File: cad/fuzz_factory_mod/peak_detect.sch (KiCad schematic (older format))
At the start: 46 parts

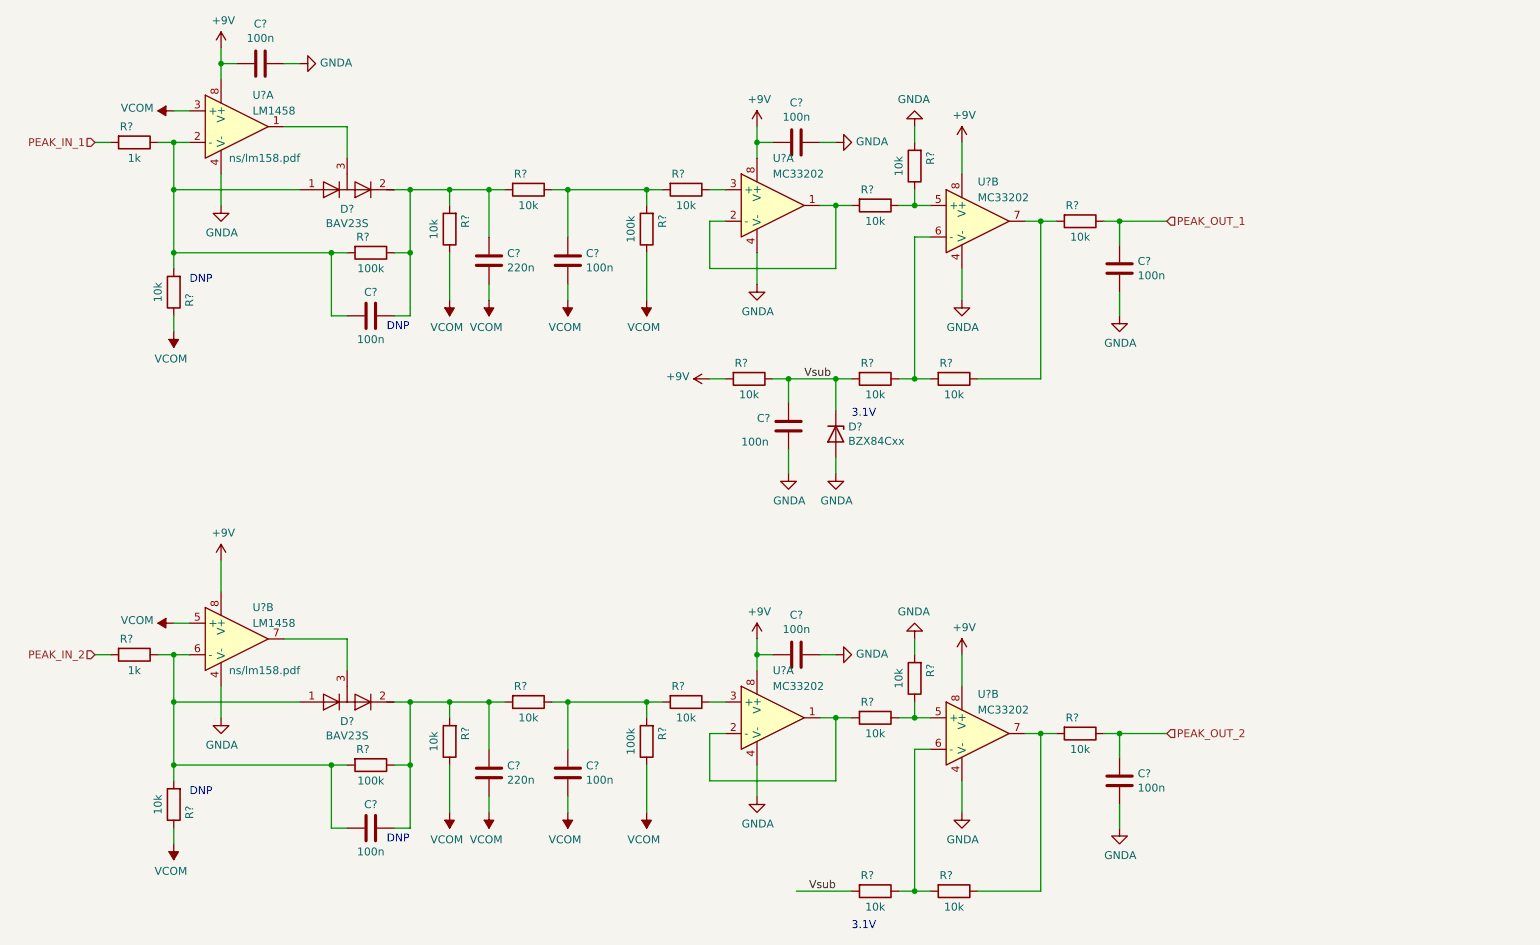
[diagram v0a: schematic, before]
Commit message: Modified OPA repartition on peak detector.
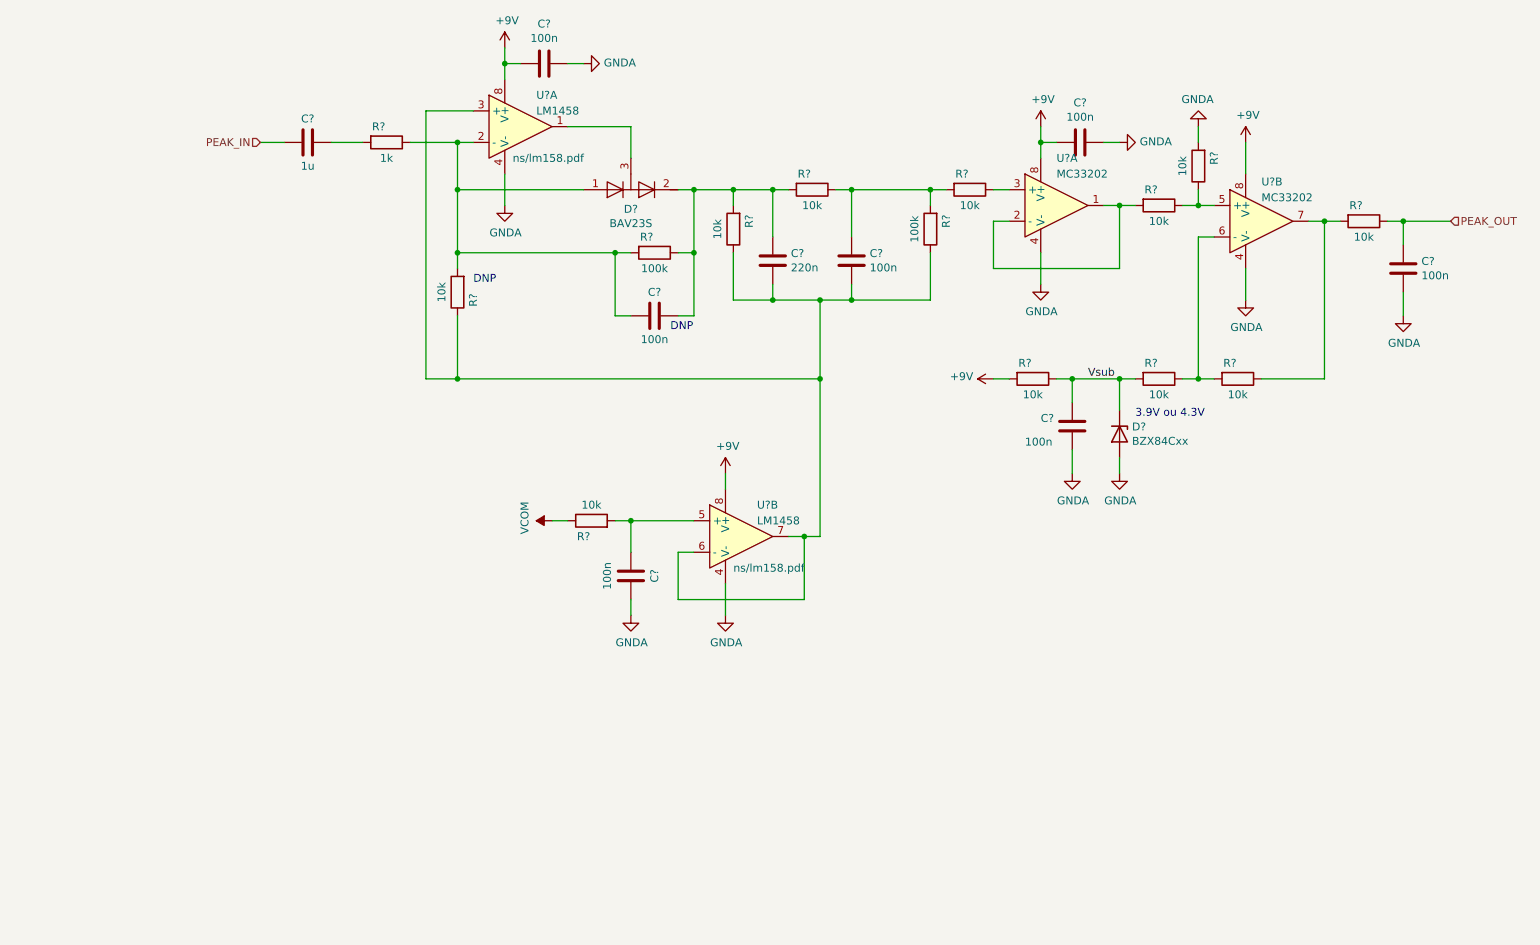
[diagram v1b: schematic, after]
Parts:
- removed C? (x4): 100n, symbol Device:C
- removed C?: 220n, symbol Device:C
- removed D?: BAV23S, symbol flax_lib:BAV23S
- removed R? (x2): 100k, symbol Device:R
- removed R?: 1k, symbol Device:R
- removed R? (x9): 10k, symbol Device:R
- removed U? (x2): MC33202, symbol flax_lib:MC33202
- added C?: 100n, symbol Device:C
- added C?: 1u, symbol Device:C
- added R?: 10k, symbol Device:R
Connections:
- net GNDA: now also C?.1
- net VCOM: now also R?.1; no longer C?.2, C?.2, R?.1, R?.1, R?.1, U?.3 (+), U?.5 (+)
- net at U?.6 (-): now also C?.2, C?.2, R?.1, R?.1, R?.1, U?.3 (+), U?.7
- net PEAK_IN_1: no longer names the net of R?.2
- net PEAK_IN_1: now also C?.1
- net PEAK_OUT_1 renamed PEAK_OUT
- new net: C?.2, R?.2, U?.5 (+)
- new net PEAK_IN: C?.2
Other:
- note added: "3.9V ou 4.3V"
- note removed: "3.1V"
- moved on the sheet: C?, D?, R?, U?A, U?B

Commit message: Continued schematic.
Modified fuuz_factory circuit : use of matched transistor pairs.
Added USB interface, through FT230X and direct to MCU.
Associated footprints, except for XTAL and trimmers.
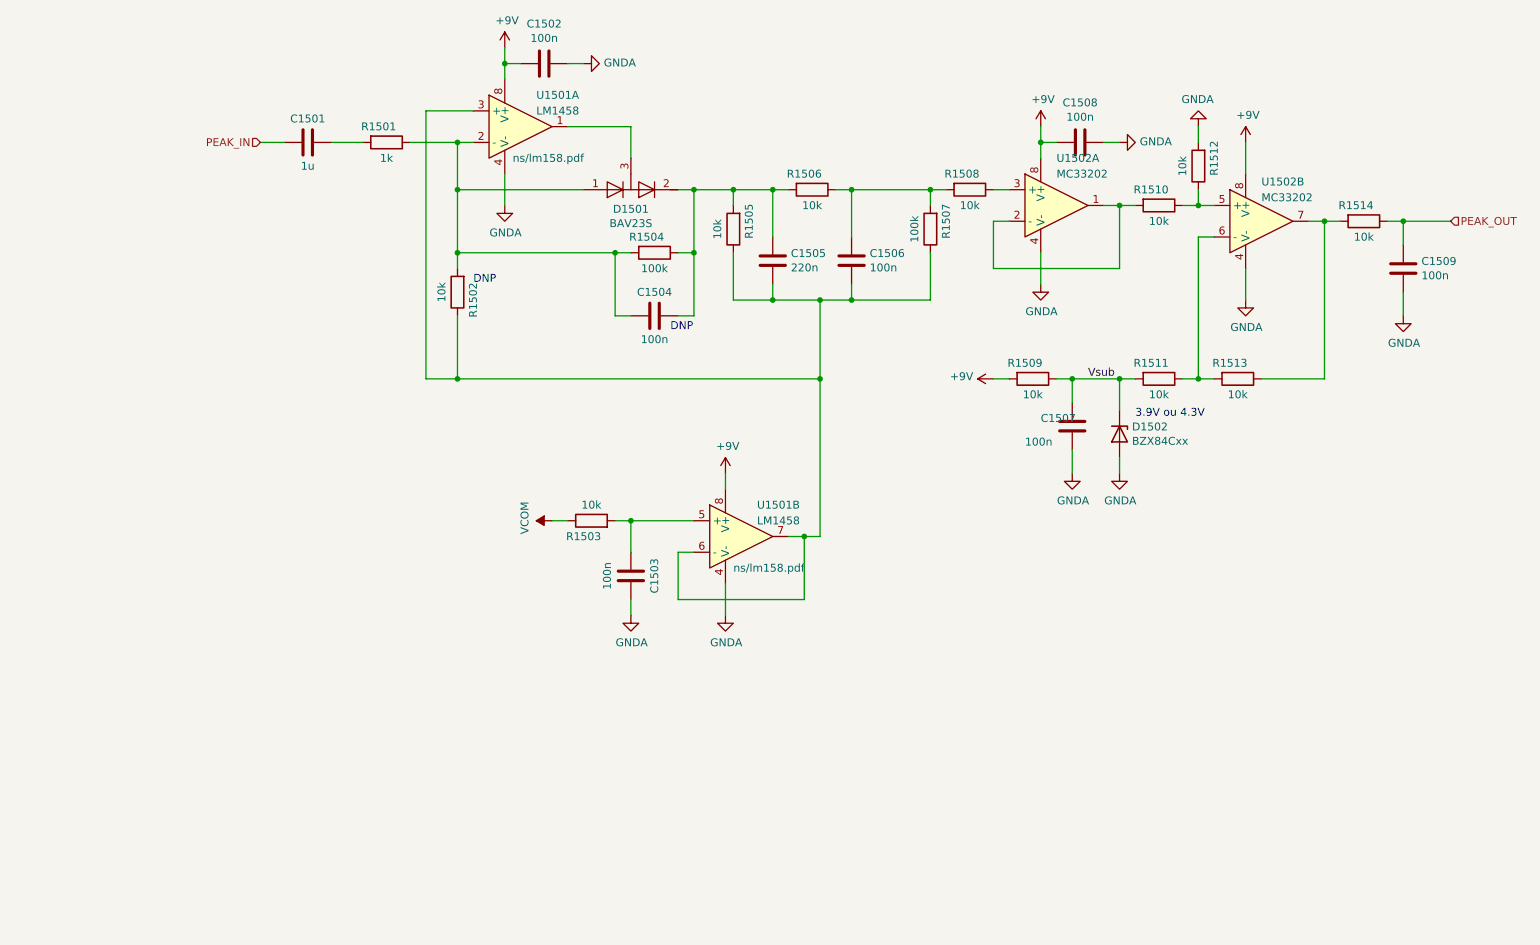
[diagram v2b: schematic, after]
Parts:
- C1101, C1105: renamed from C?; footprint (none) -> Capacitors_SMD:C_0805
- C1102, C1103, C1104, C1106, C1107, C1108, C1109: renamed from C?; footprint (none) -> Capacitors_SMD:C_0603
- D1101: renamed from D?; footprint (none) -> TO_SOT_Packages_SMD:SOT-23
- R1101, R1102, R1103, R1104, R1105, R1106, R1107, R1108, R1110, R1111, R1112, R1113, R1114: renamed from R?; footprint (none) -> Resistors_SMD:R_0603
- R1109: renamed from R?; footprint (none) -> Resistors_SMD:R_0805
- U1101, U1102: renamed from U?; footprint (none) -> Housings_SOIC:SOIC-8_3.9x4.9mm_Pitch1.27mm
- gave numbers to parts that had none: 1

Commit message: Continued schematic.
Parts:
- D1102: footprint Diode_SMD:D_SOT-23_ANK -> Diodes_SMD:D_SOT-23_ANK

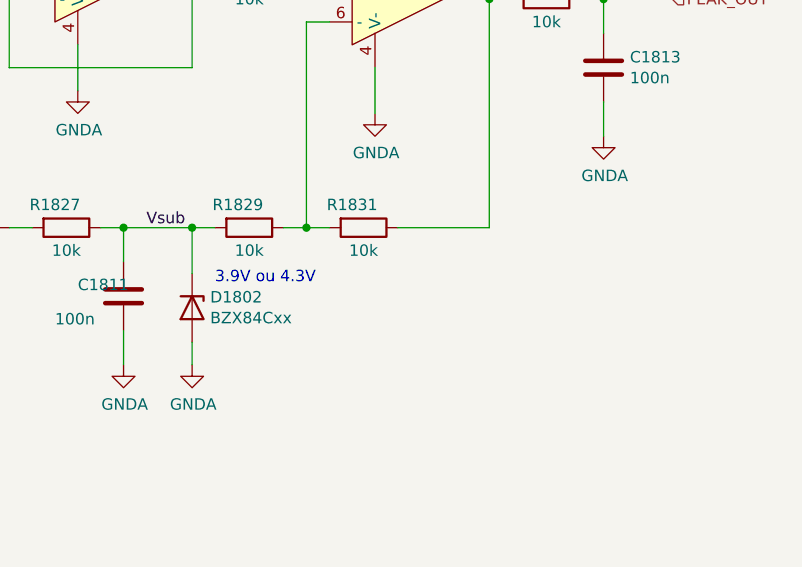
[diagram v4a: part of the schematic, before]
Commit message: Continued schematic.
Continued component placement.
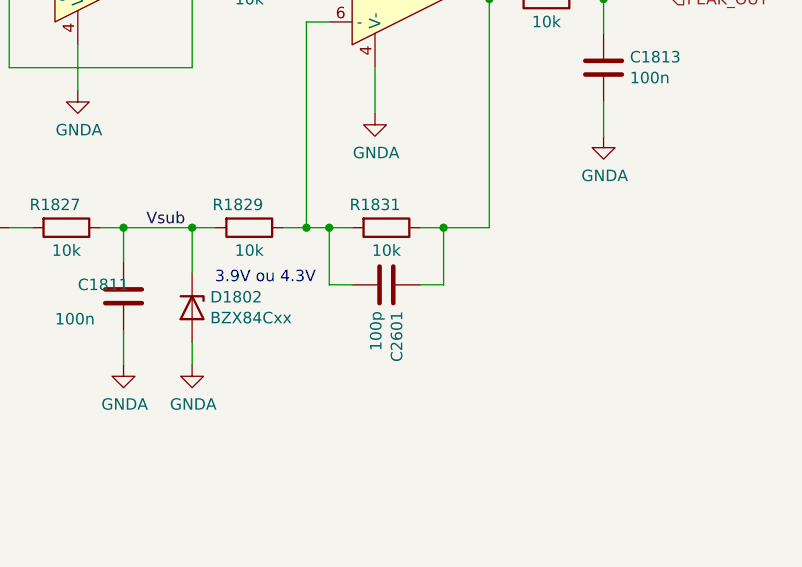
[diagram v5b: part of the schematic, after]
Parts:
- added C1901: 100p, Capacitors_SMD:C_0603, symbol Device:C
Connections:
- net at R1111.1, R1113.2, U1102.6 (-): now also C1901.2
- net at R1113.1, R1114.2, U1102.7: now also C1901.1
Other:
- moved on the sheet: R1831
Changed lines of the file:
@@
 $Descr A4 11693 8268
 encoding utf-8
-Sheet 11 30
+Sheet 19 30
 Title ""
 Date ""
@@
 L Device:R R1113
 U 1 1 5E6C867B
-P 8950 3000
+P 9050 3000
 AR Path="/5DE4AD88/5E68EE8E/5E6C867B" Ref="R1113"  Part="1"
 AR Path="/5DE4AD88/5EB8346E/5E6C867B" Ref="R1513"  Part="1"
 AR Path="/5DE4AD88/5EE3A0D9/5E6C867B" Ref="R1715"  Part="1"
 AR Path="/5DE4AD88/5EE3A870/5E6C867B" Ref="R1831"  Part="1"
-F 0 "R1831" V 8850 2950 50  0000 C CNN
-F 1 "10k" V 9050 3000 50  0000 C CNN
-F 2 "Resistors_SMD:R_0603" V 8880 3000 50  0001 C CNN
-F 3 "~" H 8950 3000 50  0001 C CNN
-	1    8950 3000
+F 0 "R1831" V 8950 2950 50  0000 C CNN
+F 1 "10k" V 9150 3000 50  0000 C CNN
+F 2 "Resistors_SMD:R_0603" V 8980 3000 50  0001 C CNN
+F 3 "~" H 9050 3000 50  0001 C CNN
+	1    9050 3000
 	0    1    1    0
 $EndComp
@@
 Connection ~ 8200 1900
 Wire Wire Line
-	8800 3000 8700 3000
-Wire Wire Line
-	9100 3000 9500 3000
-Wire Wire Line
 	9500 3000 9500 2000
 Wire Wire Line
@@
 Wire Wire Line
 	8700 2100 8700 3000
-Connection ~ 8700 3000
 Wire Wire Line
 	8700 3000 8600 3000
@@
 Wire Wire Line
 	2900 1500 2750 1500
+$Comp
+L Device:C C1901
+U 1 1 5EDFFDFD
+P 9050 3250
+AR Path="/5DE4AD88/5E68EE8E/5EDFFDFD" Ref="C1901"  Part="1"
+AR Path="/5DE4AD88/5EB8346E/5EDFFDFD" Ref="C2210"  Part="1"
+AR Path="/5DE4AD88/5EE3A0D9/5EDFFDFD" Ref="C2501"  Part="1"
+AR Path="/5DE4AD88/5EE3A870/5EDFFDFD" Ref="C2601"  Part="1"
+F 0 "C2601" H 9165 3296 50  0000 L CNN
+F 1 "100p" H 9165 3205 50  0000 L CNN
+F 2 "Capacitors_SMD:C_0603" H 9088 3100 50  0001 C CNN
+F 3 "~" H 9050 3250 50  0001 C CNN
+	1    9050 3250
+	0    1    1    0
+$EndComp
+Wire Wire Line
+	9200 3000 9300 3000
+Wire Wire Line
+	9200 3250 9300 3250
+Wire Wire Line
+	9300 3250 9300 3000
+Connection ~ 9300 3000
+Wire Wire Line
+	9300 3000 9500 3000
+Wire Wire Line
+	8900 3000 8800 3000
+Connection ~ 8700 3000
+Wire Wire Line
+	8900 3250 8800 3250
+Wire Wire Line
+	8800 3250 8800 3000
+Connection ~ 8800 3000
+Wire Wire Line
+	8800 3000 8700 3000
 $EndSCHEMATC

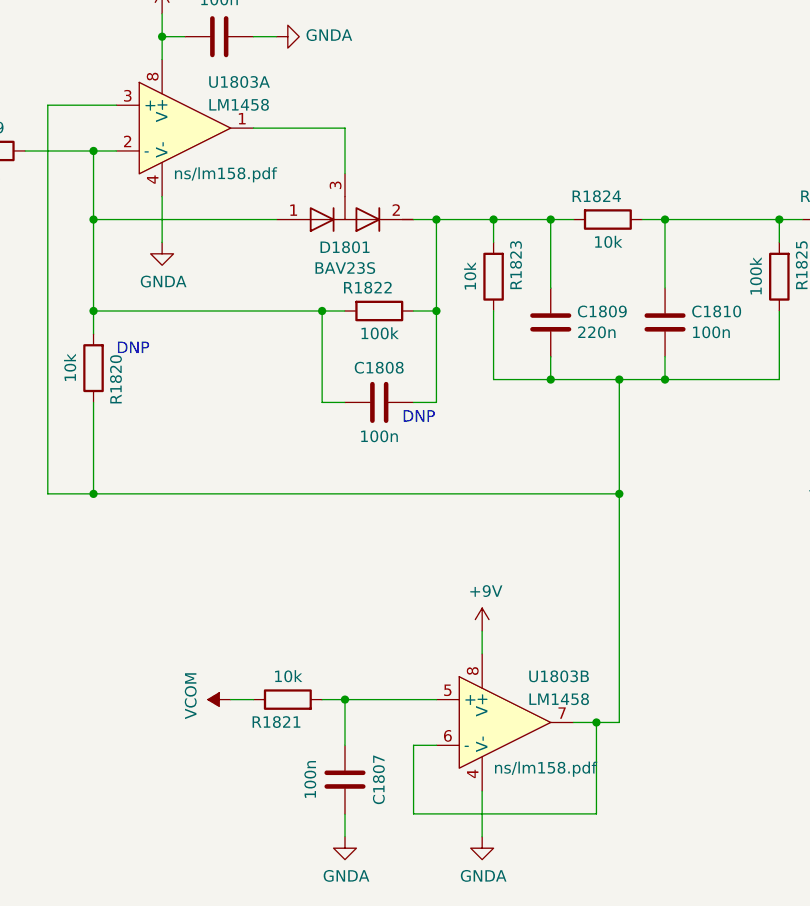
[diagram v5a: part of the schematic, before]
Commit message: Changes architecture.
Corrections on schematic.
Continued Layout placement.
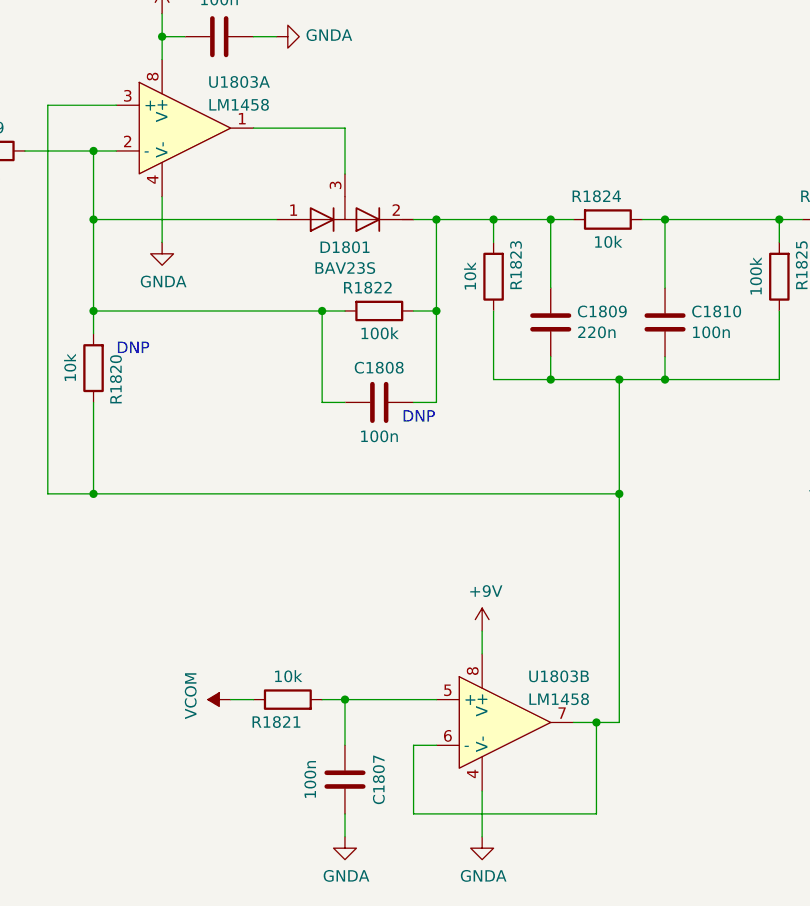
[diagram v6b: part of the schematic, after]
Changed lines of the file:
@@
 $Descr A4 11693 8268
 encoding utf-8
-Sheet 19 30
+Sheet 19 22
 Title ""
 Date ""
@@
 F 1 "LM1458" H 4500 1500 50  0000 L CNN
 F 2 "Housings_SOIC:SOIC-8_3.9x4.9mm_Pitch1.27mm" H 4400 1400 50  0001 C CNN
-F 3 "ns/lm158.pdf" H 4350 1200 50  0000 L CNN
+F 3 "" H 4350 1200 50  0000 L CNN
 	1    4400 1400
 	1    0    0    -1
@@
 F 1 "LM1458" H 5900 4100 50  0000 L CNN
 F 2 "Housings_SOIC:SOIC-8_3.9x4.9mm_Pitch1.27mm" H 5800 4000 50  0001 C CNN
-F 3 "ns/lm158.pdf" H 5750 3800 50  0000 L CNN
+F 3 "" H 5750 3800 50  0001 L CNN
 	2    5800 4000
 	1    0    0    -1

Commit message: Continued layout.
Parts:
- removed R1109: 10k, Resistors_SMD:R_0805, symbol Device:R
- added R1318: 10k, Resistors_SMD:R_0603, symbol Device:R
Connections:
- net +9V: now also R1318.2
- net Vsub: now also R1318.1
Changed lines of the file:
@@
 EESchema Schematic File Version 4
-LIBS:fuzz_factory_mod-cache
 EELAYER 30 0
 EELAYER END
 $Descr A4 11693 8268
 encoding utf-8
-Sheet 19 22
+Sheet 18 22
 Title ""
 Date ""
@@
 Wire Wire Line
 	8200 3000 8200 3200
-$Comp
-L Device:R R1109
-U 1 1 5E6DCF38
-P 7650 3000
-AR Path="/5DE4AD88/5E68EE8E/5E6DCF38" Ref="R1109"  Part="1"
-AR Path="/5DE4AD88/5EB8346E/5E6DCF38" Ref="R1509"  Part="1"
-AR Path="/5DE4AD88/5EE3A0D9/5E6DCF38" Ref="R1711"  Part="1"
-AR Path="/5DE4AD88/5EE3A870/5E6DCF38" Ref="R1827"  Part="1"
-F 0 "R1827" V 7550 2950 50  0000 C CNN
-F 1 "10k" V 7750 3000 50  0000 C CNN
-F 2 "Resistors_SMD:R_0805" V 7580 3000 50  0001 C CNN
-F 3 "~" H 7650 3000 50  0001 C CNN
-	1    7650 3000
-	0    1    1    0
-$EndComp
 Connection ~ 8200 3000
 $Comp
@@
 Wire Wire Line
 	8800 3000 8700 3000
+$Comp
+L Device:R R1318
+U 1 1 5F717D12
+P 7650 3000
+AR Path="/5DE4AD88/5E68EE8E/5F717D12" Ref="R1318"  Part="1"
+AR Path="/5DE4AD88/5EB8346E/5F717D12" Ref="R1601"  Part="1"
+AR Path="/5DE4AD88/5EE3A0D9/5F717D12" Ref="R1801"  Part="1"
+AR Path="/5DE4AD88/5EE3A870/5F717D12" Ref="R1901"  Part="1"
+F 0 "R1901" V 7550 2950 50  0000 C CNN
+F 1 "10k" V 7750 3000 50  0000 C CNN
+F 2 "Resistors_SMD:R_0603" V 7580 3000 50  0001 C CNN
+F 3 "~" H 7650 3000 50  0001 C CNN
+	1    7650 3000
+	0    1    1    0
+$EndComp
 $EndSCHEMATC
